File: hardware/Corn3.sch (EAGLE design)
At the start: 67 parts, among them IC1 STM32F10XCXT6, J1 JTAG-MINI-SH, J4 M04-PICOBLADE, U1 DRV8303, U2 LTC3630A, U3 AS1362

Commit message: Add diode from USB V+ to +5V (#1).
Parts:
- added D1: (no value), dan-diode:D-SMA
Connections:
- new net N$10: D1.A, JP3.VBUS
- net +5V: now also D1.C
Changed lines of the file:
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@@
 <part name="P-7" library="supply1" deviceset="V-" device=""/>
 <part name="C17" library="Xo-RCL" deviceset="CPOL-US" device="-E3,5-8" value="470uF/35V"/>
+<part name="D1" library="dan-diode" deviceset="D" device="-SMA"/>
+<part name="P+11" library="supply1" deviceset="+5V" device=""/>
 </parts>
 <sheets>
@@
 <instance part="P+6" gate="1" x="78.74" y="55.88"/>
 <instance part="JP3" gate="G$1" x="83.82" y="124.46"/>
+<instance part="D1" gate="G$1" x="63.5" y="139.7" rot="R90"/>
+<instance part="P+11" gate="1" x="63.5" y="149.86"/>
 </instances>
 <busses>
@@
 <wire x1="86.36" y1="45.72" x2="78.74" y2="45.72" width="0.1524" layer="91"/>
 <wire x1="78.74" y1="45.72" x2="78.74" y2="53.34" width="0.1524" layer="91"/>
+</segment>
+<segment>
+<pinref part="P+11" gate="1" pin="+5V"/>
+<pinref part="D1" gate="G$1" pin="C"/>
+<wire x1="63.5" y1="147.32" x2="63.5" y2="142.24" width="0.1524" layer="91"/>
 </segment>
 </net>
@@
 </segment>
 </net>
+<net name="N$10" class="0">
+<segment>
+<pinref part="D1" gate="G$1" pin="A"/>
+<pinref part="JP3" gate="G$1" pin="VBUS"/>
+<wire x1="63.5" y1="137.16" x2="63.5" y2="127" width="0.1524" layer="91"/>
+<wire x1="63.5" y1="127" x2="81.28" y2="127" width="0.1524" layer="91"/>
+</segment>
+</net>

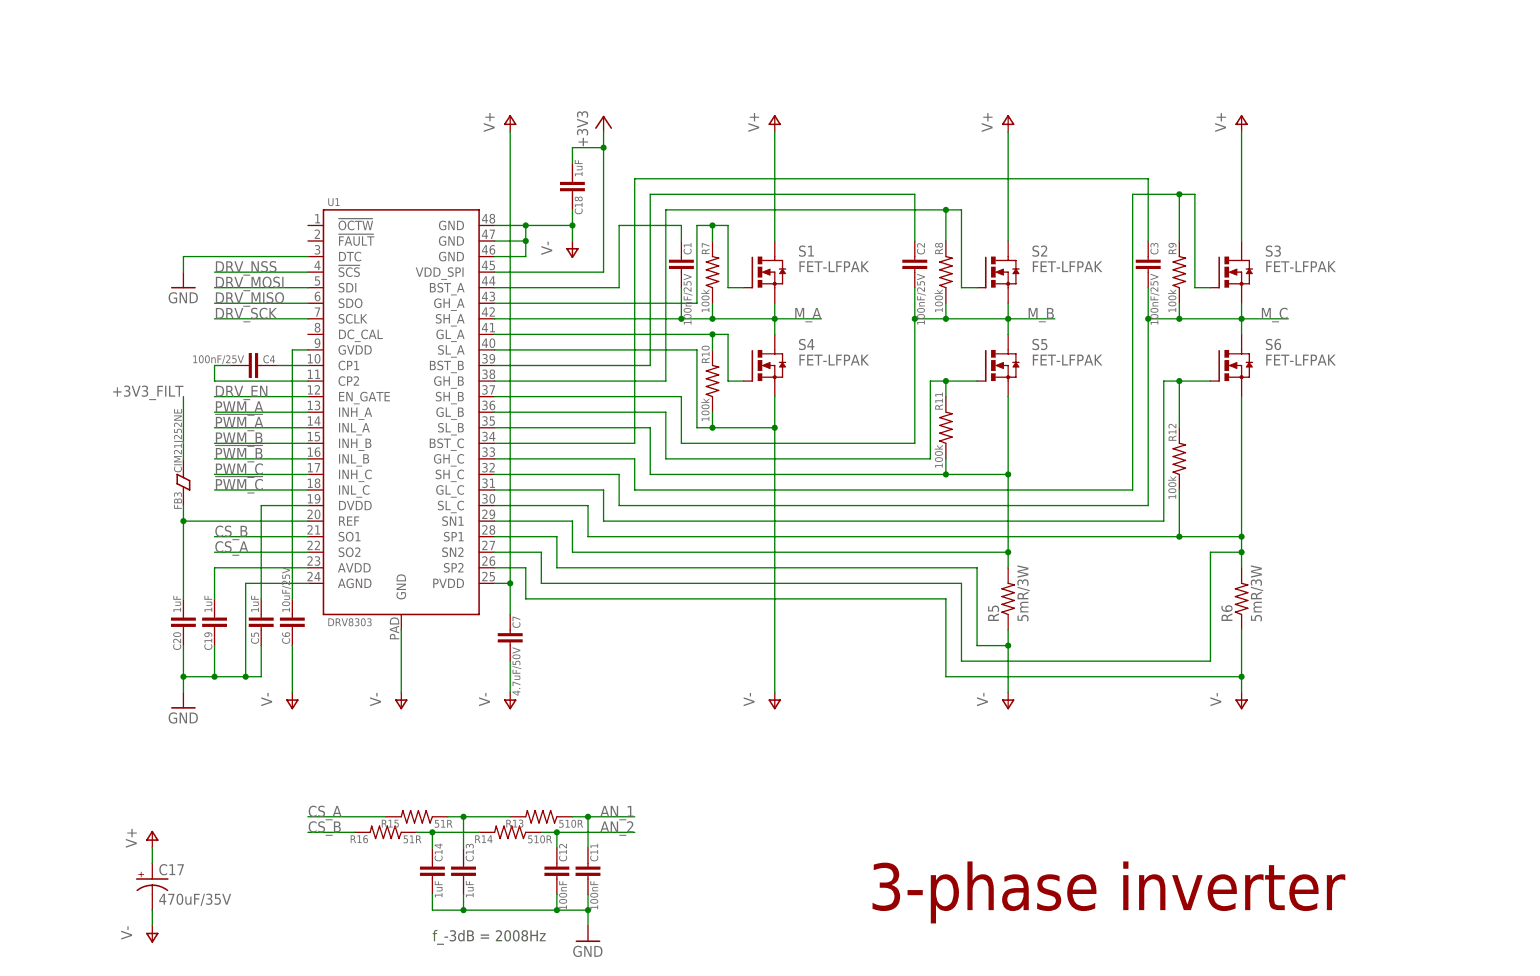
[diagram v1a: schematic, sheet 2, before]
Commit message: Add completed hardware v3.2 (#1, #4, #23, #24, #25).
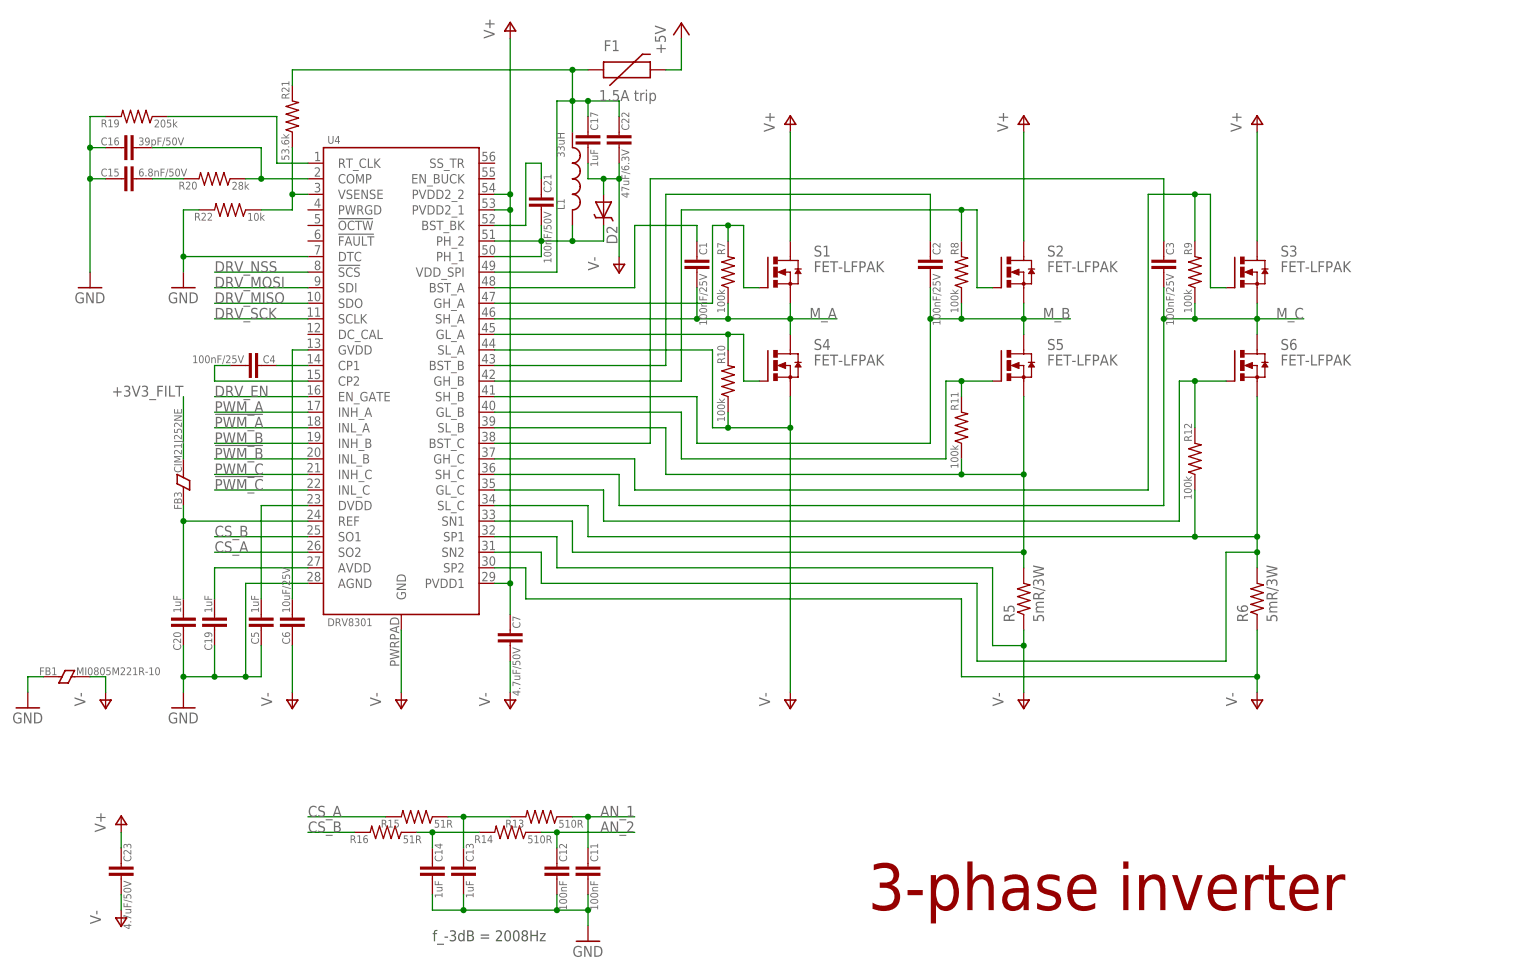
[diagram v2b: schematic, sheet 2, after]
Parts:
- removed C18: 1uF, dan-rcl:C0603
- removed U1: DRV8303, Xo-Driver:DRV8303
- removed U2: LTC3630A, Xo-VReg:LTC3630A
- added C21: 100nF/50V, dan-rcl:C0603
- added C22: 47uF/6.3V, dan-rcl:C0805
- added C23: 4.7uF/50V, dan-rcl:C1206
- added D2: DIODE-SCHOTTKY_, SparkFun-DiscreteSemi:DIODE-SCHOTTKY_
- added R19: 205k, dan-rcl:R0603
- added R20: 28k, dan-rcl:R0603
- added R21: 53.6k, dan-rcl:R0603
- added R22: 10k, dan-rcl:R0603
- added U4: DRV8301, Xo-Driver:DRV8301
- C15: value 4.7uF/50V -> 6.8nF/50V; device dan-rcl:C1206 -> dan-rcl:C0603
- C16: value 100uF/6.3V -> 39pF/50V; device dan-rcl:C1206 -> dan-rcl:C0603
- C17: value 470uF/35V -> 1uF; device Xo-RCL:CPOL-US-E3,5-8 -> dan-rcl:C0603
- C8: value 100uF/6.3V -> 22uF; device dan-rcl:C1206 -> dan-rcl:C0805
- D1: value (none) -> DIODE-SCHOTTKY; device dan-diode:D-SMA -> SparkFun-DiscreteSemi:DIODE-SCHOTTKY
- J1: value JTAG-MINI-SH -> JTAG-MINI; device Xo-Connector:JTAG-MINI-SH -> Xo-Connector:JTAG-MINI
- J4: value M04-PICOBLADE -> PICOBLADE-UART-PORT; device Xo-Connector:M04-PICOBLADE -> Xo-Connector:PICOBLADE-UART-PORT
- JP1: value (none) -> HALL_SENSOR_CONNECTOR_SM4A; device pinhead-2:PINHD-1X05_2.54-S -> Xo-Connector:HALL_SENSOR_CONNECTOR_SM4A
- JP2: value (none) -> FLEXIPORT_HORI; device pinhead-2:PINHD-1X04_2.54-S -> Xo-Connector:FLEXIPORT_HORI
- L1: value 22uH/1A -> 33uH; device Xo-RCL:L-US_NR50 -> Xo-RCL:L-US_NR40
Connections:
- removed net AN_3: IC1PORTB_L.PB2
- removed net N$16: R11.1, R5.2, S5.S, U1.SL_B, U1.SN1
- removed net N$17: R12.1, R6.2, S6.S, U1.SL_C, U1.SN2
- new net N$12: C21.1, U4.BST_BK
- new net N$19: C17.1, C22.1, F1.1, L1.1, R21.2, U4.VDD_SPI
- new net N$20: C16.2, R20.1, U4.COMP
- new net N$33: R19.1, U4.RT_CLK
- new net SL_B: R11.1, R5.2, S5.S, U4.SL_B, U4.SN1
- new net SL_C: R12.1, R6.2, S6.S, U4.SL_C, U4.SN2
- net !PWM_A: now also U4.INL_A; no longer U1.INL_A
- net !PWM_B: now also U4.INL_B; no longer U1.INL_B
- net !PWM_C: now also U4.INL_C; no longer U1.INL_C
- net +3V3: no longer C18.2, U1.VDD_SPI
- net +5V: now also JP1.+5V, JP2.PWR; no longer JP1.1, JP2.2
- net CS_A: now also U4.SO2; no longer U1.SO2
- net CS_B: now also U4.SO1; no longer U1.SO1
- net DRV_EN: now also U4.EN_GATE; no longer U1.EN_GATE
- net DRV_MISO: now also U4.SDO; no longer U1.SDO
- net DRV_MOSI: now also U4.SDI; no longer U1.SDI
- net DRV_NSS: now also IC1PORTB_H.PB8, U4.!SCS; no longer IC1PORTB_L.PB6, U1.!SCS
- net DRV_SCK: now also U4.SCLK; no longer U1.SCLK
- net GND: now also C16.1, JP1.GND, JP2.GND, R19.2, R22.2, U4.AGND, U4.DTC; no longer C16.2, JP1.2, JP2.1, U1.AGND, U1.DTC, U2.GND, U2.VPRG2
- net HALL_A: now also JP1.A; no longer JP1.3
- net HALL_B: now also JP1.B; no longer JP1.4
- net HALL_C: now also JP1.C; no longer JP1.5
- net I2C_SCL: now also IC1PORTB_L.PB6, JP2.TX/SCL; no longer IC1PORTB_H.PB8, JP2.4
- net I2C_SDA: now also IC1PORTB_L.PB7, JP2.RX/SDA; no longer IC1PORTB_H.PB9, JP2.3
- net LEDX: now also IC1PORTB_H.PB9; no longer IC1PORTB_L.PB7
- net M_A: now also U4.SH_A; no longer U1.SH_A
- net M_B: now also U4.SH_B; no longer U1.SH_B
- net M_C: now also U4.SH_C; no longer U1.SH_C
- net N$13: now also U4.BST_A; no longer U1.BST_A
- net N$14: now also U4.BST_B; no longer U1.BST_B
- net N$15: now also U4.BST_C; no longer U1.BST_C
- net N$18: now also U4.GL_A; no longer U1.GL_A
- net N$23: now also C15.2, R20.2; no longer U2.SS, U2.VPRG1
- net N$24: now also R21.1, R22.1, U4.VSENSE; no longer L1.2, U2.SW
- net N$25: now also U4.DVDD; no longer U1.DVDD
- net N$26: now also U4.GVDD; no longer U1.GVDD
- net N$27: now also U4.CP1; no longer U1.CP1
- net N$28: now also U4.CP2; no longer U1.CP2
- net N$29: now also C21.2, D2.C, L1.2, U4.PH_1, U4.PH_2; no longer C16.1, F1.1, L1.1, U2.VFB
- net N$3: now also U4.GH_B; no longer U1.GH_B
- net N$31: now also U4.REF; no longer U1.REF
- net N$32: now also U4.AVDD; no longer U1.AVDD
- net N$4: now also U4.GH_A; no longer U1.GH_A
- net N$6: now also U4.GL_C; no longer U1.GL_C
- net N$7: now also U4.GL_B; no longer U1.GL_B
- net N$9: now also U4.GH_C; no longer U1.GH_C
- net PWM_A: now also U4.INH_A; no longer U1.INH_A
- net PWM_B: now also U4.INH_B; no longer U1.INH_B
- net PWM_C: now also U4.INH_C; no longer U1.INH_C
- net V+: now also C23.1, U4.PVDD1, U4.PVDD2_1, U4.PVDD2_2; no longer C15.2, C17.+, U1.PVDD, U2.VIN
- net V-: now also C17.2, C22.2, C23.2, D2.A, U4.GND, U4.SL_A, U4.SP1, U4.SP2; no longer C17.-, C18.1, U1.GND, U1.GND@1, U1.GND@2, U1.GND@3, U1.SL_A, U1.SP1, U1.SP2
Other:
- moved on the sheet: C1, C2, C3, J4, R10, R11, R12, R5, R6, R7, R8, R9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
